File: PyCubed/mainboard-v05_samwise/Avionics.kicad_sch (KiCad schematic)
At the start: 27 parts, among them SW1 KMR231NG LFS, U1 MAX706RESA, U2 ATSAMD51J20A-AU, Y1 32.768kHz

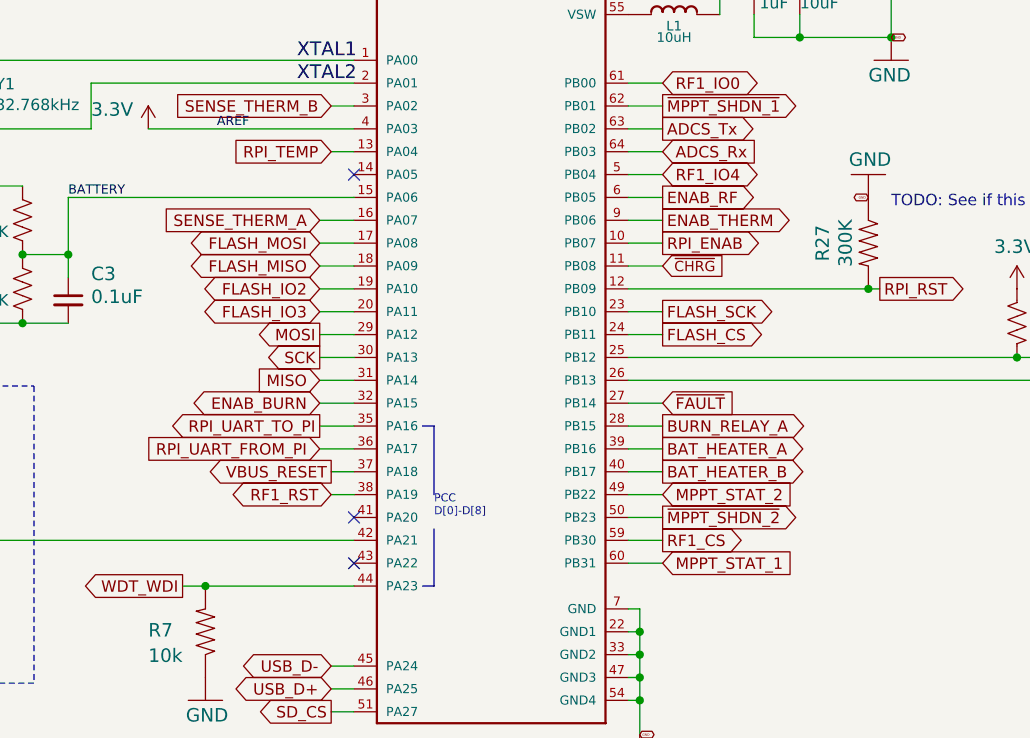
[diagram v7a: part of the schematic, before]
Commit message: Lots of changes
ADCS connector size increased
X solar panel connectors now have burn connection
Added second burn mosfet output
Touched up RF LDO regulator
Fliped RPi UART signals
Likely some other small things.
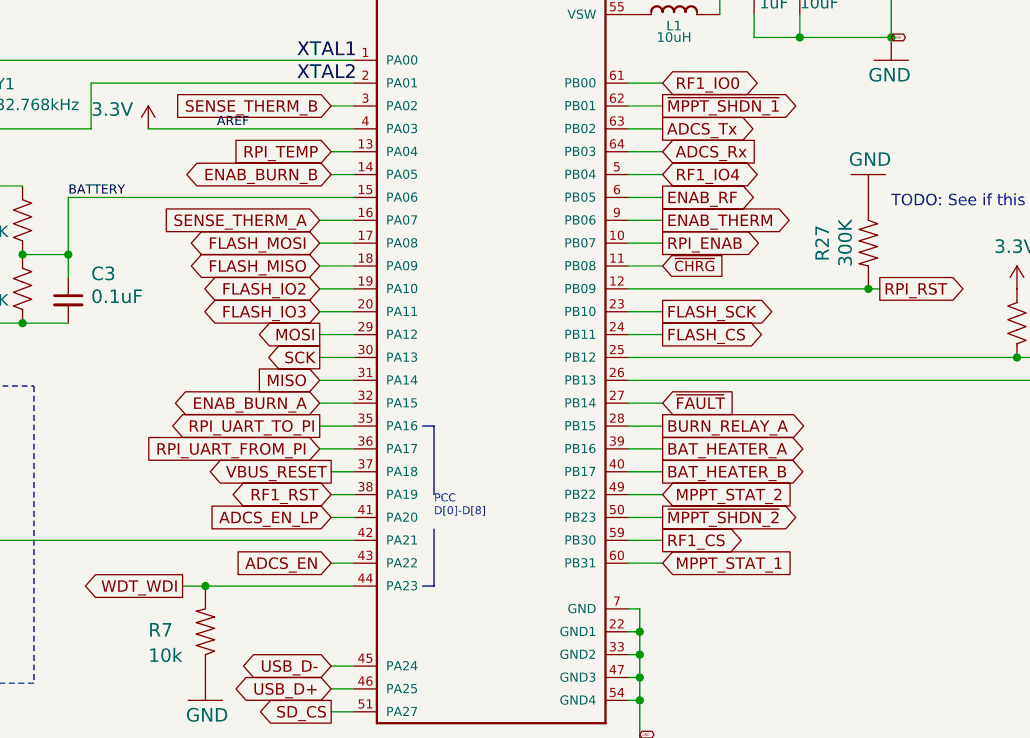
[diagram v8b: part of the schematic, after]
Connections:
- net ENAB_BURN_B: now reaches U2.14 (PA05)
- net ADCS_EN_LP: now reaches U2.41 (PA20)
- net ADCS_EN: now reaches U2.43 (PA22)
- net ENAB_BURN renamed ENAB_BURN_A
- no-connect marks 5 -> 2
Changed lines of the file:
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@@
   (junction (at 137.16 85.09) (diameter 0) (color 0 0 0 0)
   )
-  (no_connect (at 92.71 161.29))
   (no_connect (at 64.77 43.18))
   (no_connect (at 34.29 158.75))
-  (no_connect (at 92.71 156.21))
-  (no_connect (at 92.71 118.11))
   (wire (pts (xy 78.74 77.47) (xy 81.28 77.47))
     (stroke (width 0) (type default))
@@
     (stroke (width 0) (type default))
   )
+  (wire (pts (xy 90.17 118.11) (xy 92.71 118.11))
+    (stroke (width 0) (type default))
+  )
   (wire (pts (xy 123.19 130.81) (xy 149.86 130.81))
     (stroke (width 0) (type default))
@@
     (stroke (width 0) (type default))
   )
+  (wire (pts (xy 90.17 161.29) (xy 92.71 161.29))
+    (stroke (width 0) (type default))
+  )
   (wire (pts (xy 123.19 153.67) (xy 127 153.67))
     (stroke (width 0) (type default))
@@
   )
   (wire (pts (xy 137.16 92.71) (xy 132.08 92.71))
+    (stroke (width 0) (type default))
+  )
+  (wire (pts (xy 90.17 156.21) (xy 92.71 156.21))
     (stroke (width 0) (type default))
   )
@@
     )
   )
-  (global_label "GND" (shape bidirectional) (at 149.86 120.65 180) (fields_autoplaced)
-    (effects (font (size 0.254 0.254)) (justify right))
-    (property "Intersheetrefs" "${INTERSHEET_REFS}" (at 24.13 92.71 0)
-      (effects (font (size 1.27 1.27)) hide)
+  (global_label "ENAB_BURN_B" (shape bidirectional) (at 90.17 118.11 180) (fields_autoplaced)
+    (effects (font (size 1.27 1.27)) (justify right))
+    (property "Intersheetrefs" "${INTERSHEET_REFS}" (at 73.6422 118.11 0)
+      (effects (font (size 1.27 1.27)) (justify right) hide)
+    )
+  )
+  (global_label "ADCS_EN" (shape input) (at 90.17 161.29 180) (fields_autoplaced)
+    (effects (font (size 1.27 1.27)) (justify right))
+    (property "Intersheetrefs" "${INTERSHEET_REFS}" (at 79.5538 161.29 0)
+      (effects (font (size 1.27 1.27)) (justify right) hide)
     )
   )
@@
     )
   )
-  (global_label "ENAB_BURN" (shape bidirectional) (at 88.9 143.51 180) (fields_autoplaced)
-    (effects (font (size 1.27 1.27)) (justify right))
-    (property "Intersheetrefs" "${INTERSHEET_REFS}" (at 74.6892 143.51 0)
+  (global_label "ENAB_BURN_A" (shape bidirectional) (at 88.9 143.51 180) (fields_autoplaced)
+    (effects (font (size 1.27 1.27)) (justify right))
+    (property "Intersheetrefs" "${INTERSHEET_REFS}" (at 72.5536 143.51 0)
       (effects (font (size 1.27 1.27)) (justify right) hide)
     )
@@
       (effects (font (size 1.27 1.27)) (justify right) hide)
     )
+  )
+  (global_label "ADCS_EN_LP" (shape input) (at 90.17 156.21 180) (fields_autoplaced)
+    (effects (font (size 1.27 1.27)) (justify right))
+    (property "Intersheetrefs" "${INTERSHEET_REFS}" (at 76.2881 156.21 0)
+      (effects (font (size 1.27 1.27)) (justify right) hide)
+    )
